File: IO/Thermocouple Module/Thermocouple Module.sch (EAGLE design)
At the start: 25 parts, among them U1 74HC541, U2 74HC541

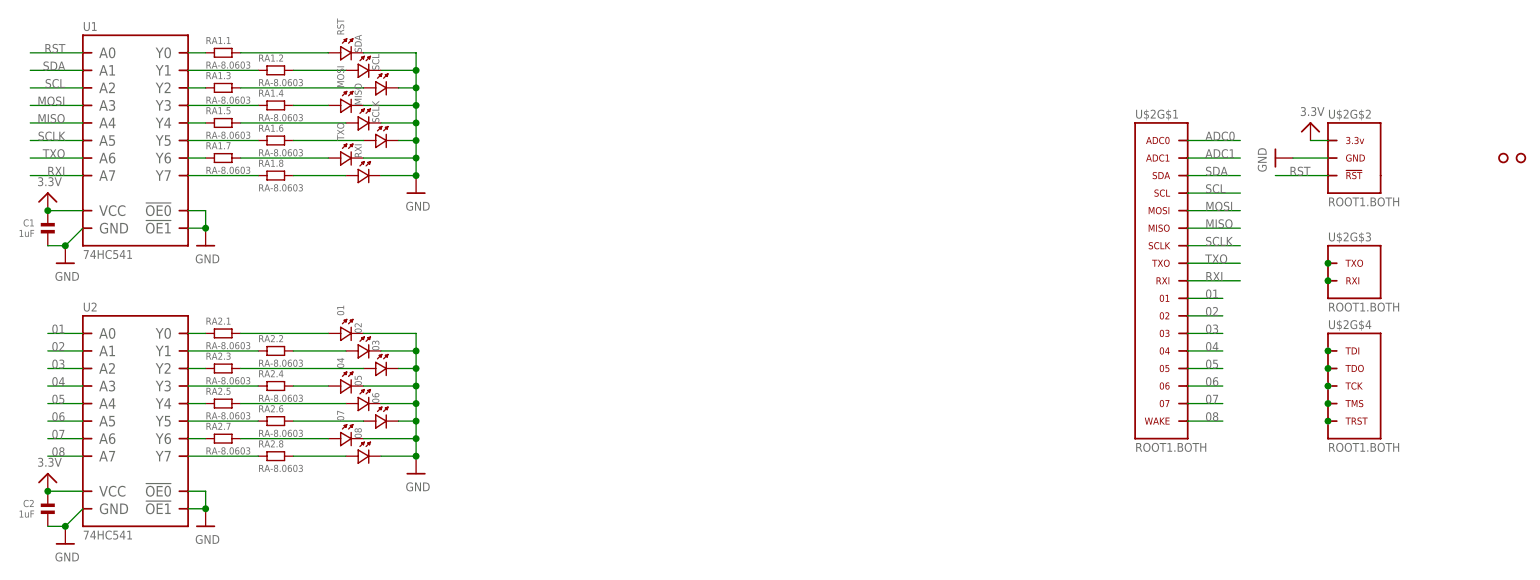
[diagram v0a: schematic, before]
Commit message: Completed Debug Module Added/began Thermocouple Module
Signed-off-by: Cruz Monrreal II <Cruz.Monrreal@gmail.com>
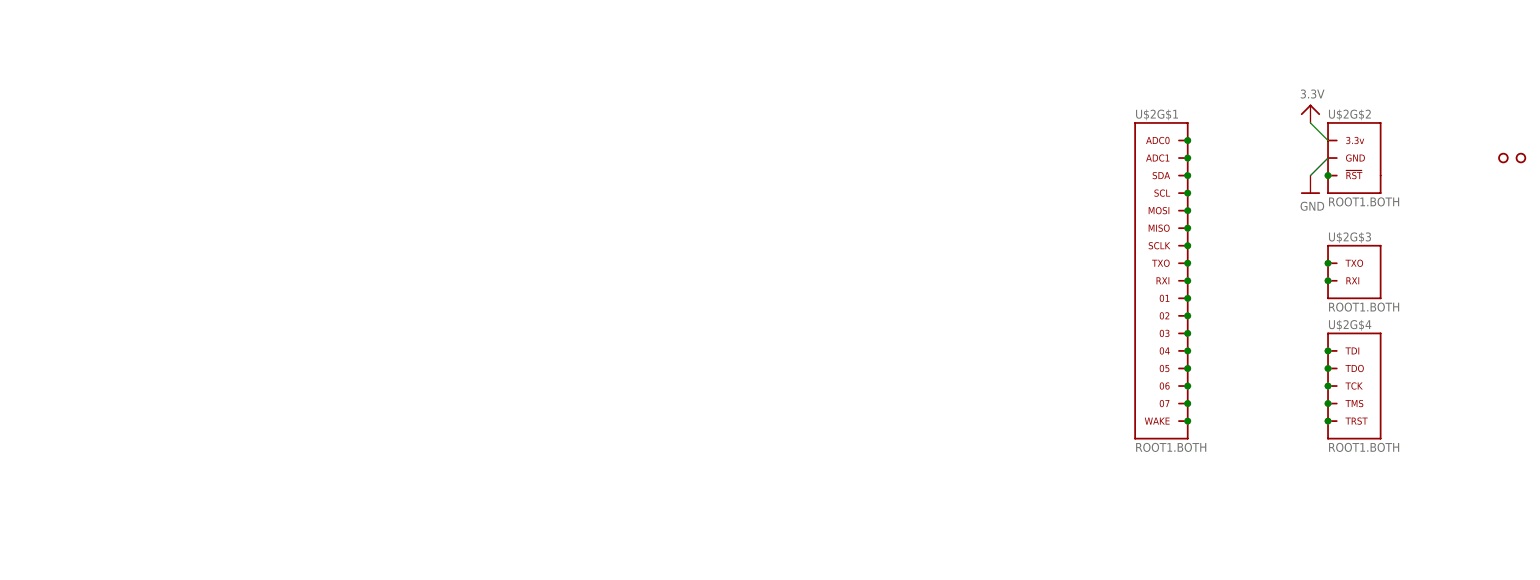
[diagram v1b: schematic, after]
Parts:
- removed 01, 02, 03, 04, 05, 06, 07, 08, MISO, MOSI, RST, RXI, SCL, SCLK, SDA, TXO: (no value), .standardparts:LED.0603
- removed C1, C2: 1uF, .standardparts:CAPACITOR.0603
- removed RA1, RA2: RA-8.0603, .resistorarray:RA-8.0603
- removed U1, U2: 74HC541, nxp:74HC541
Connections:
- net ADC0 renamed N$13
- net ADC1 renamed N$2
- removed net 01: U$2G$1.01, U2.A0
- removed net 02: U$2G$1.02, U2.A1
- removed net 03: U$2G$1.03, U2.A2
- removed net 04: U$2G$1.04, U2.A3
- removed net 05: U$2G$1.05, U2.A4
- removed net 06: U$2G$1.06, U2.A5
- removed net 07: U$2G$1.07, U2.A6
- removed net 08: U$2G$1.WAKE, U2.A7
- removed net MISO: U$2G$1.MISO, U1.A4
- removed net MOSI: U$2G$1.MOSI, U1.A3
- removed net N$13 (its old number): 05.1, RA2.5.2
- removed net N$2 (its old number): RA2.1.1, U2.Y0
- removed net N$51: RA1.1.1, U1.Y0
- removed net N$52: RA1.2.1, U1.Y1
- removed net N$53: RA1.3.1, U1.Y2
- removed net N$54: RA1.4.1, U1.Y3
- removed net N$55: RA1.5.1, U1.Y4
- removed net N$56: RA1.6.1, U1.Y5
- removed net N$57: RA1.7.1, U1.Y6
- removed net N$58: RA1.8.1, U1.Y7
- removed net N$59: RA1.7.2, TXO.1
- removed net N$60: RA1.8.2, RXI.1
- removed net N$61: RA1.6.2, SCLK.1
- removed net N$62: MISO.1, RA1.5.2
- removed net N$63: MOSI.1, RA1.4.2
- removed net N$64: RA1.3.2, SCL.1
- removed net N$65: RA1.2.2, SDA.1
- removed net N$66: RA1.1.2, RST.1
- removed net RST: U$2G$2.!RST, U1.A0
- removed net RXI: U$2G$1.RXI, U1.A7
- removed net SCL: U$2G$1.SCL, U1.A2
- removed net SCLK: U$2G$1.SCLK, U1.A5
- removed net SDA: U$2G$1.SDA, U1.A1
- removed net TXO: U$2G$1.TXO, U1.A6
- new net N$1: U$2G$1.04
- new net N$25: U$2G$2.!RST
- net 3.3V: no longer C1.1, C2.1, U1.VCC, U2.VCC
- net GND: no longer 01.2, 02.2, 03.2, 04.2, 05.2, 06.2, 07.2, 08.2, C1.2, C2.2, MISO.2, MOSI.2, RST.2, RXI.2, SCL.2, SCLK.2, SDA.2, TXO.2, U1.!OE0!, U1.!OE1!, U1.GND, U2.!OE0!, U2.!OE1!, U2.GND
- net N$10: now also U$2G$1.01; no longer 07.1, RA2.7.2
- net N$11: now also U$2G$1.02; no longer 08.1, RA2.8.2
- net N$12: now also U$2G$1.MOSI; no longer 06.1, RA2.6.2
- net N$14: now also U$2G$1.05; no longer 04.1, RA2.4.2
- net N$15: now also U$2G$1.06; no longer 03.1, RA2.3.2
- net N$16: now also U$2G$1.07; no longer 02.1, RA2.2.2
- net N$17: now also U$2G$1.WAKE; no longer 01.1, RA2.1.2
- net N$3: now also U$2G$1.SDA; no longer RA2.2.1, U2.Y1
- net N$4: now also U$2G$1.SCL; no longer RA2.3.1, U2.Y2
- net N$5: now also U$2G$1.03; no longer RA2.4.1, U2.Y3
- net N$6: now also U$2G$1.MISO; no longer RA2.5.1, U2.Y4
- net N$7: now also U$2G$1.SCLK; no longer RA2.6.1, U2.Y5
- net N$8: now also U$2G$1.TXO; no longer RA2.7.1, U2.Y6
- net N$9: now also U$2G$1.RXI; no longer RA2.8.1, U2.Y7

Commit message: Completed Thermocouple Module
Signed-off-by: Cruz Monrreal II <Cruz.Monrreal@gmail.com>
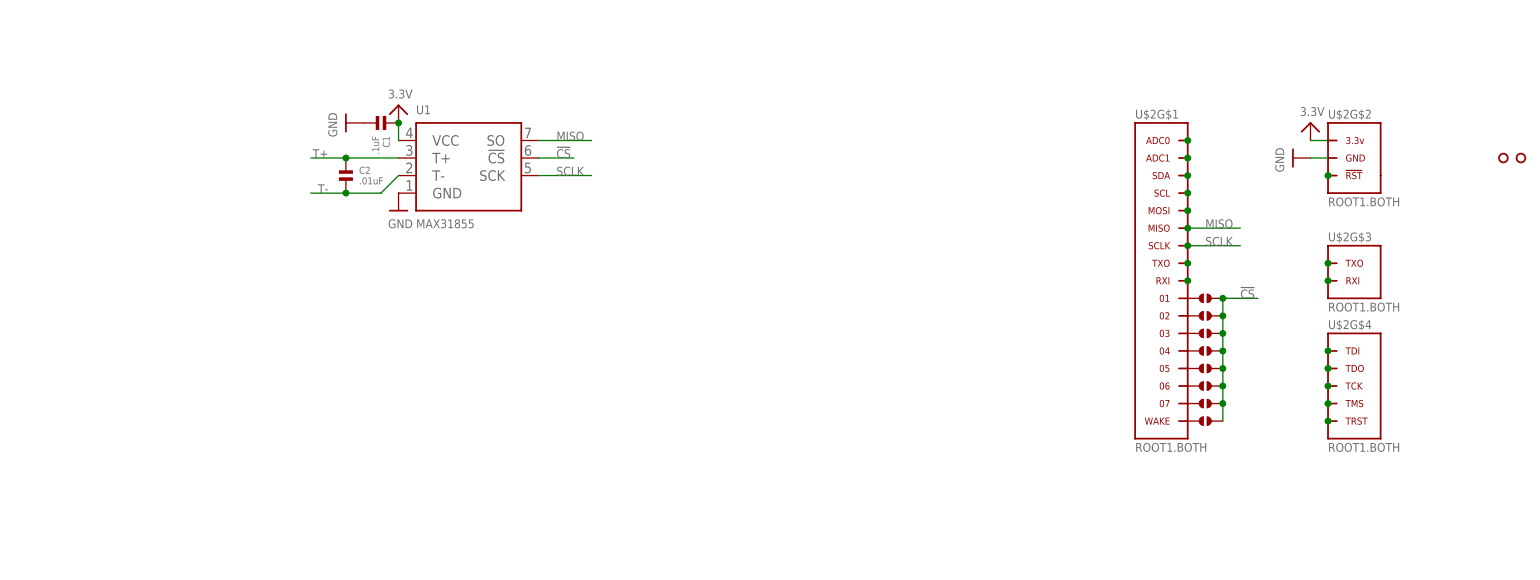
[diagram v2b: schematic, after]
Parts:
- added C1: .1uF, .standardparts:CAPACITOR.0603
- added C2: .01uF, .standardparts:CAPACITOR.0603
- added J1, J2, J3, J4, J5, J6, J7, J8: (no value), .solderjumper:SOLDERJUMPER.2.SML
- added U1: MAX31855, maxim:MAX31855
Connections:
- removed net N$6: U$2G$1.MISO
- removed net N$7: U$2G$1.SCLK
- new net !CS: J1.2, J2.2, J3.2, J4.2, J5.2, J6.2, J7.2, J8.2, U1.!CS
- new net MISO: U$2G$1.MISO, U1.SO
- new net SCLK: U$2G$1.SCLK, U1.SCK
- new net T+: C2.1, U1.T+
- new net T-: C2.2, U1.T-
- net 3.3V: now also C1.1, U1.VCC
- net GND: now also C1.2, U1.GND
- net N$1: now also J1.1, U$2G$1.01; no longer U$2G$1.04
- net N$10: now also J3.1, U$2G$1.03; no longer U$2G$1.01
- net N$11: now also J4.1, U$2G$1.04; no longer U$2G$1.02
- net N$14: now also J5.1
- net N$15: now also J6.1
- net N$16: now also J7.1
- net N$17: now also J8.1
- net N$5: now also J2.1, U$2G$1.02; no longer U$2G$1.03
